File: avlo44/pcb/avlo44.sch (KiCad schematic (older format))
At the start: 102 parts, among them P1 OLED, SW1 SW_PUSH, SW10 SW_PUSH, SW11 SW_PUSH, SW12 SW_PUSH, SW13 SW_PUSH, SW14 SW_PUSH, SW15 SW_PUSH, SW16 SW_PUSH, SW17 SW_PUSH, SW18 SW_PUSH, SW19 SW_PUSH, SW2 SW_PUSH, SW20 SW_PUSH, SW21 SW_PUSH, SW22 SW_PUSH, SW25 SW_PUSH, SW26 SW_PUSH, SW27 SW_PUSH, SW28 SW_PUSH, SW29 SW_PUSH, SW3 SW_PUSH, SW30 SW_PUSH, SW31 SW_PUSH, SW32 SW_PUSH, SW33 SW_PUSH, SW34 SW_PUSH, SW35 SW_PUSH, SW36 SW_PUSH, SW37 SW_PUSH, SW38 SW_PUSH, SW39 SW_PUSH, SW4 SW_PUSH, SW40 SW_PUSH, SW41 SW_PUSH, SW42 SW_PUSH, SW43 SW_PUSH, SW44 SW_PUSH, SW45 SW_PUSH, SW46 SW_PUSH, SW5 SW_PUSH, SW6 SW_PUSH, SW7 SW_PUSH, SW8 SW_PUSH, SW9 SW_PUSH, U1 ProMicro

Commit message: Initial routing complete for Avlo44
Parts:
- removed L11: WS2812B, avlo-parts:WS2812B, symbol LED:WS2812B
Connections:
- net col0: now also SW37.1
- net col1: now also SW38.1
- net col2: now also SW39.1
- net col3: now also SW40.1
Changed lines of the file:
@@
 	1    0    0    -1
 $EndComp
-$Comp
-L LED:WS2812B L11
-U 1 1 5DF0B8C4
-P 9450 6950
-F 0 "L11" H 9794 6996 50  0000 L CNN
-F 1 "WS2812B" H 9794 6905 50  0000 L CNN
-F 2 "avlo-parts:WS2812B" H 9500 6650 50  0001 L TNN
-F 3 "https://cdn-shop.adafruit.com/datasheets/WS2812B.pdf" H 9550 6575 50  0001 L TNN
-	1    9450 6950
-	1    0    0    -1
-$EndComp
-NoConn ~ 9750 6950
 Wire Wire Line
 	3250 6650 3450 6650
@@
 Connection ~ 8250 6650
 Wire Wire Line
-	8850 6650 9450 6650
-Connection ~ 8850 6650
-Wire Wire Line
 	3250 7250 3450 7250
 Wire Wire Line
@@
 	8250 7250 8850 7250
 Connection ~ 8250 7250
-Wire Wire Line
-	8850 7250 9450 7250
-Connection ~ 8850 7250
 $Comp
 L Diode:1N4148W D46
@@
 row7
 Wire Wire Line
-	3300 4600 3300 5850
-Wire Wire Line
-	4300 4600 4300 5850
-Wire Wire Line
-	5300 4600 5300 5850
-Wire Wire Line
-	6300 4600 6300 5850
+	3300 4600 3300 5250
+Wire Wire Line
+	4300 4600 4300 5250
+Wire Wire Line
+	5300 4600 5300 5250
+Wire Wire Line
+	6300 4600 6300 5250
 Text GLabel 2500 2550 2    50   Input ~ 0
 row7
@@
 	7300 4600 7300 5250
 Connection ~ 7300 4600
+NoConn ~ 9150 6950
+Connection ~ 3300 5250
+Wire Wire Line
+	3300 5250 3300 5850
+Connection ~ 4300 5250
+Wire Wire Line
+	4300 5250 4300 5850
+Connection ~ 5300 5250
+Wire Wire Line
+	5300 5250 5300 5850
+Connection ~ 6300 5250
+Wire Wire Line
+	6300 5250 6300 5850
 $EndSCHEMATC

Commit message: Update mounting holes, add artwork and add production files
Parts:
- added TH1, TH10, TH11, TH2, TH3, TH4, TH5, TH6, TH7, TH8, TH9: HOLE, avlo-parts:HOLE_M2_TH, symbol Lily58-rescue:HOLE-Lily58-cache
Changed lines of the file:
@@
 Wire Wire Line
 	6300 5250 6300 5850
+$Comp
+L Lily58-rescue:HOLE-Lily58-cache TH1
+U 1 1 60A38A4E
+P 3450 8600
+F 0 "TH1" H 3450 8400 60  0000 C CNN
+F 1 "HOLE" H 3450 8300 60  0000 C CNN
+F 2 "avlo-parts:HOLE_M2_TH" H 3450 8600 60  0001 C CNN
+F 3 "" H 3450 8600 60  0000 C CNN
+	1    3450 8600
+	1    0    0    -1
+$EndComp
+$Comp
+L Lily58-rescue:HOLE-Lily58-cache TH2
+U 1 1 60A3CEF3
+P 3850 8600
+F 0 "TH2" H 3850 8400 60  0000 C CNN
+F 1 "HOLE" H 3850 8300 60  0000 C CNN
+F 2 "avlo-parts:HOLE_M2_TH" H 3850 8600 60  0001 C CNN
+F 3 "" H 3850 8600 60  0000 C CNN
+	1    3850 8600
+	1    0    0    -1
+$EndComp
+$Comp
+L Lily58-rescue:HOLE-Lily58-cache TH3
+U 1 1 60A40957
+P 4250 8600
+F 0 "TH3" H 4250 8400 60  0000 C CNN
+F 1 "HOLE" H 4250 8300 60  0000 C CNN
+F 2 "avlo-parts:HOLE_M2_TH" H 4250 8600 60  0001 C CNN
+F 3 "" H 4250 8600 60  0000 C CNN
+	1    4250 8600
+	1    0    0    -1
+$EndComp
+$Comp
+L Lily58-rescue:HOLE-Lily58-cache TH4
+U 1 1 60A441AC
+P 4650 8600
+F 0 "TH4" H 4650 8400 60  0000 C CNN
+F 1 "HOLE" H 4650 8300 60  0000 C CNN
+F 2 "avlo-parts:HOLE_M2_TH" H 4650 8600 60  0001 C CNN
+F 3 "" H 4650 8600 60  0000 C CNN
+	1    4650 8600
+	1    0    0    -1
+$EndComp
+$Comp
+L Lily58-rescue:HOLE-Lily58-cache TH5
+U 1 1 60A47B88
+P 5050 8600
+F 0 "TH5" H 5050 8400 60  0000 C CNN
+F 1 "HOLE" H 5050 8300 60  0000 C CNN
+F 2 "avlo-parts:HOLE_M2_TH" H 5050 8600 60  0001 C CNN
+F 3 "" H 5050 8600 60  0000 C CNN
+	1    5050 8600
+	1    0    0    -1
+$EndComp
+$Comp
+L Lily58-rescue:HOLE-Lily58-cache TH6
+U 1 1 60A4B300
+P 5550 8600
+F 0 "TH6" H 5550 8400 60  0000 C CNN
+F 1 "HOLE" H 5550 8300 60  0000 C CNN
+F 2 "avlo-parts:HOLE_M2_TH" H 5550 8600 60  0001 C CNN
+F 3 "" H 5550 8600 60  0000 C CNN
+	1    5550 8600
+	1    0    0    -1
+$EndComp
+$Comp
+L Lily58-rescue:HOLE-Lily58-cache TH7
+U 1 1 60A4EBFF
+P 5950 8600
+F 0 "TH7" H 5950 8400 60  0000 C CNN
+F 1 "HOLE" H 5950 8300 60  0000 C CNN
+F 2 "avlo-parts:HOLE_M2_TH" H 5950 8600 60  0001 C CNN
+F 3 "" H 5950 8600 60  0000 C CNN
+	1    5950 8600
+	1    0    0    -1
+$EndComp
+$Comp
+L Lily58-rescue:HOLE-Lily58-cache TH8
+U 1 1 60A5297C
+P 6350 8600
+F 0 "TH8" H 6350 8400 60  0000 C CNN
+F 1 "HOLE" H 6350 8300 60  0000 C CNN
+F 2 "avlo-parts:HOLE_M2_TH" H 6350 8600 60  0001 C CNN
+F 3 "" H 6350 8600 60  0000 C CNN
+	1    6350 8600
+	1    0    0    -1
+$EndComp
+$Comp
+L Lily58-rescue:HOLE-Lily58-cache TH9
+U 1 1 60A5626A
+P 6750 8600
+F 0 "TH9" H 6750 8400 60  0000 C CNN
+F 1 "HOLE" H 6750 8300 60  0000 C CNN
+F 2 "avlo-parts:HOLE_M2_TH" H 6750 8600 60  0001 C CNN
+F 3 "" H 6750 8600 60  0000 C CNN
+	1    6750 8600
+	1    0    0    -1
+$EndComp
+$Comp
+L Lily58-rescue:HOLE-Lily58-cache TH10
+U 1 1 60A59BAD
+P 7150 8600
+F 0 "TH10" H 7150 8400 60  0000 C CNN
+F 1 "HOLE" H 7150 8300 60  0000 C CNN
+F 2 "avlo-parts:HOLE_M2_TH" H 7150 8600 60  0001 C CNN
+F 3 "" H 7150 8600 60  0000 C CNN
+	1    7150 8600
+	1    0    0    -1
+$EndComp
+$Comp
+L Lily58-rescue:HOLE-Lily58-cache TH11
+U 1 1 60ABB60F
+P 7650 8600
+F 0 "TH11" H 7650 8400 60  0000 C CNN
+F 1 "HOLE" H 7650 8300 60  0000 C CNN
+F 2 "avlo-parts:HOLE_M2_TH" H 7650 8600 60  0001 C CNN
+F 3 "" H 7650 8600 60  0000 C CNN
+	1    7650 8600
+	1    0    0    -1
+$EndComp
 $EndSCHEMATC

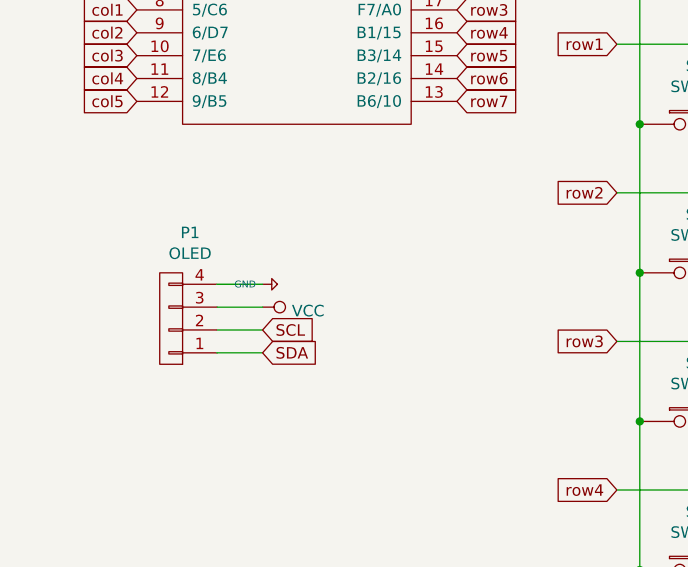
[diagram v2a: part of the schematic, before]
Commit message: Fix missing trace and add switch footprint for Kailh socket
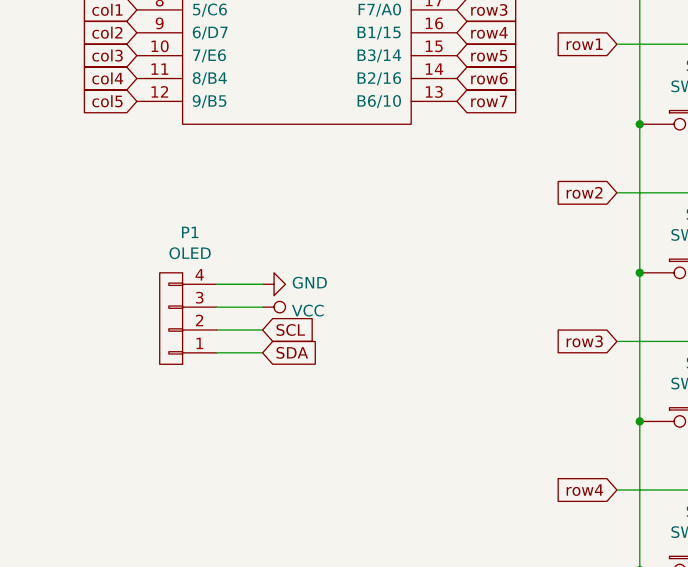
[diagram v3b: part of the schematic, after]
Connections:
- net +5V is gone; now on net GND: P1.4 (P4)
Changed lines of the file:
@@
-$EndComp
-$Comp
-L keyboard_parts:GND #PWR0101
-U 1 1 60A1ACE6
-P 1650 3350
-F 0 "#PWR0101" H 1650 3400 20  0001 C CNN
-F 1 "GND" V 1650 3379 30  0000 L CNN
-F 2 "" H 1650 3350 60  0000 C CNN
-F 3 "" H 1650 3350 60  0000 C CNN
-	1    1650 3350
-	0    -1   -1   0
 $EndComp
 $Comp
@@
 $EndComp
 Wire Wire Line
-	1450 3350 1650 3350
-Wire Wire Line
 	1450 3450 1650 3450
 Wire Wire Line
@@
 	1    0    0    -1
 $EndComp
+Wire Wire Line
+	1450 3350 1650 3350
+$Comp
+L power:GND #PWR?
+U 1 1 60B41A07
+P 1650 3350
+F 0 "#PWR?" H 1650 3100 50  0001 C CNN
+F 1 "GND" V 1655 3222 50  0000 R CNN
+F 2 "" H 1650 3350 50  0001 C CNN
+F 3 "" H 1650 3350 50  0001 C CNN
+	1    1650 3350
+	0    -1   -1   0
+$EndComp
 $EndSCHEMATC
